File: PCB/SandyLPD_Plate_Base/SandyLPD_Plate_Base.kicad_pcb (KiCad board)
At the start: 2 copper layers, 131 x 83 mm, 78 parts

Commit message: 不要部品削除
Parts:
- removed G***: LOGO, locallib:SandyLP_QR_360dpi
- removed LOGO1: Logo_Base, locallib:SandyLP_logo_LP40_w60
- removed the REF** at (63.8, 81.4)
- removed the REF** at (14.5, 44.3)
- removed the REF** at (107.9, 111.1)
- removed the REF** at (290.6, 44.5)
- removed the REF** at (161.1, 97.0)
- removed the REF** at (209.1, 44.5)
- removed the REF** at (190.1, 14.5)
- removed the REF** at (161.6, 46.6)
- removed the REF** at (269.9, 18.1)
- removed the REF** at (97.4, 22.1)
- removed the REF** at (270.5, 19.6)
- removed the REF** at (97.4, 22.0)
- removed the REF** at (308.0, 47.0)
- removed the REF** at (125.3, 60.8)
- removed the REF** at (308.8, 53.8)
- removed the REF** at (92.0, 130.3)
- removed the REF** at (209.1, 44.6)
- removed the REF** at (110.6, 24.6)
- removed the REF** at (305.1, 37.1)
- removed the REF** at (121.1, 24.6)
- removed the REF** at (159.5, 88.1)
- removed the REF** at (63.3, 81.5)
- removed the REF** at (18.1, 119.3)
- removed the REF** at (121.6, 26.2)
- removed the REF** at (190.6, 16.1)
- removed the REF** at (194.1, 60.8)
- removed the REF** at (4.39, 31.8)
- removed the REF** at (14.0, 51.6)
- removed the REF** at (254.4, 81.5)
- removed the REF** at (158.7, 95.8)
- removed the REF** at (14.6, 44.4)
- removed the REF** at (34.2, 27.6)
- removed the REF** at (305.6, 38.8)
- removed the REF** at (307.8, 111.7)
- removed the REF** at (54.9, 5.36)
- removed the REF** at (54.5, 3.76)
- removed the REF** at (261.0, 37.1)
- removed the REF** at (4.78, 33.4)
- removed the REF** at (159.8, 80.6)
- removed the REF** at (124.6, 59.2)
- removed the REF** at (309.2, 55.6)
- removed the REF** at (111.0, 26.4)
- removed the REF** at (188.2, -4.82)
- removed the REF** at (190.4, 1.58)
- removed the REF** at (209.1, 111.1)
- removed the REF** at (115.1, 26.1)
- removed the REF** at (261.5, 38.8)
- removed the REF** at (193.7, 59.2)
- removed the REF** at (206.2, 132.1)
- removed the REF** at (34.5, 29.9)
- removed the REF** at (14.5, 53.2)
- removed the REF** at (159.4, 78.8)
- removed the REF** at (114.5, 24.6)
- removed the REF** at (16.8, 117.8)
- removed the REF** at (305.6, 114.2)
- removed the REF** at (254.3, 81.4)
- removed the REF** at (159.2, 44.3)
- removed the REF** at (159.7, 87.9)
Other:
- board text removed: "#SandyLP_kbd DN0010, Base by @jpskenn github.com/jpskenn/SandyLP"
- board text removed: "100x100mm"
- board text removed: "Back Side"
- board text removed: "Fairness, Justice, Rightness"
- board text removed: "Screw for SW-plate"
- board text removed: "Screw for Top plate"
- board text removed: "Through-hole tap head diameter"

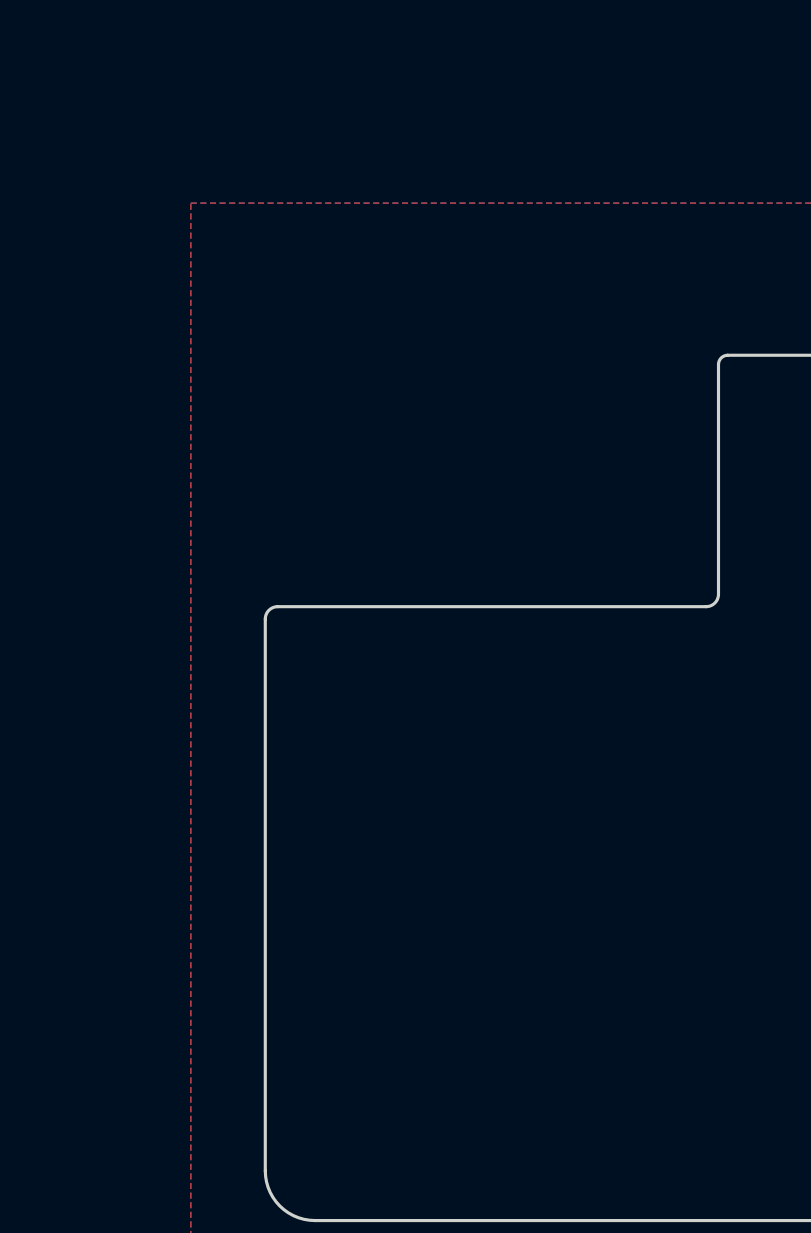
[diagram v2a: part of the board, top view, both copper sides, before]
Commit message: ロータリーエンコーダの穴をちょっと小さく。 #40
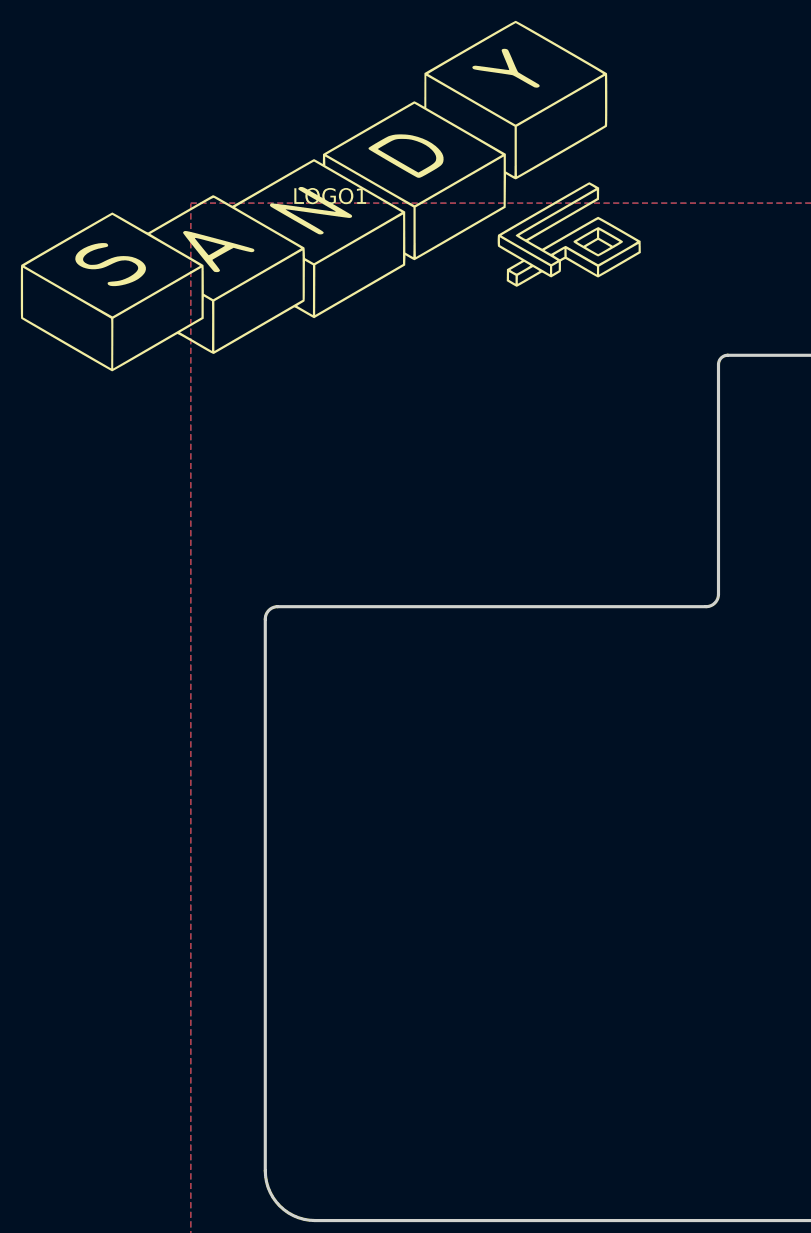
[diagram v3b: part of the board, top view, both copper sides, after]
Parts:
- added LOGO1: Logo_Base, locallib:SandyLP_logo_LP40_w60, F.Cu at (29.7, 16.9)
- SW_13: footprint locallib:MX-Switch-Hole-for-RE(higher hole)-with-narrow-frame -> locallib:MX-Switch-Hole-for-RE(higher hole)-with-narrow-frame-gentle-corner
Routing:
- added copper zone on B.Cu, net (none)
- added copper zone on F.Cu, net (none)
- removed copper zone on B.Cu, net GND
- removed copper zone on F.Cu, net GND

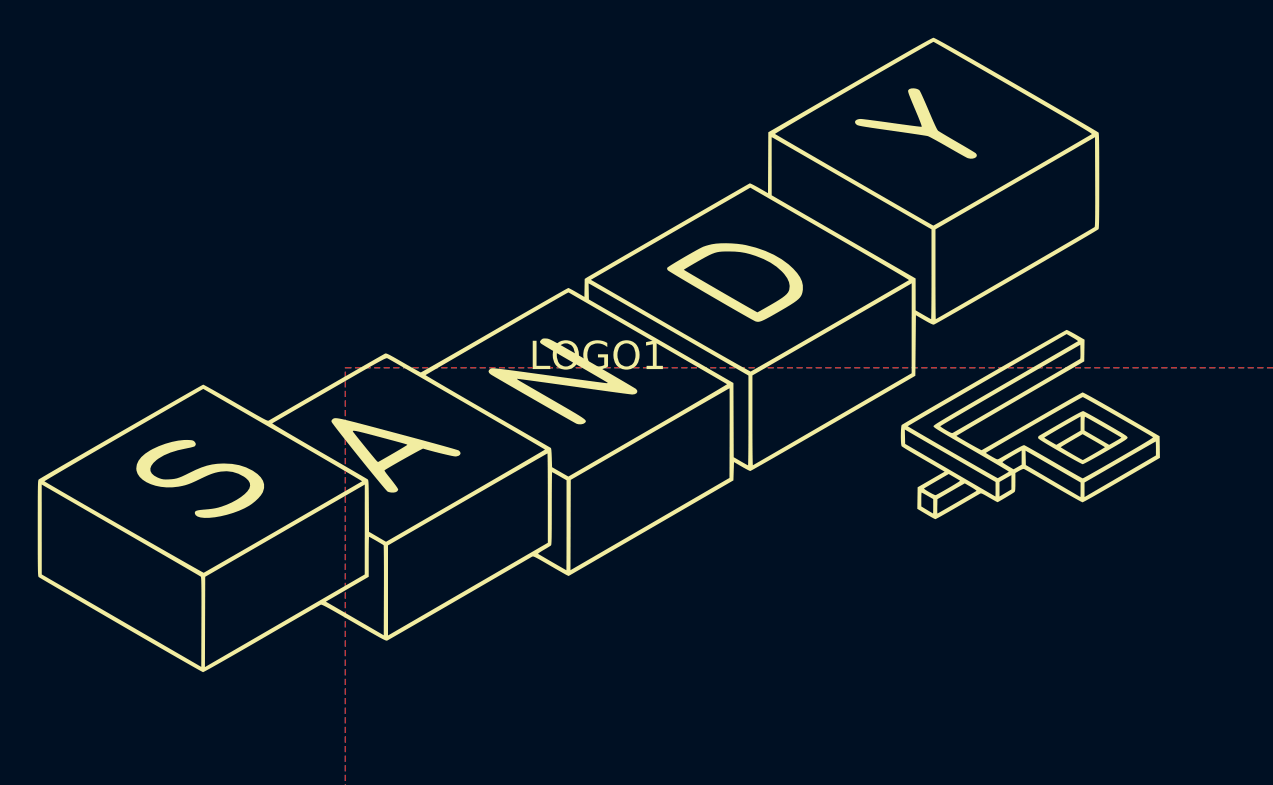
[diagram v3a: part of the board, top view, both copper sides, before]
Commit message: ゴムシート貼り付けめやすを追加
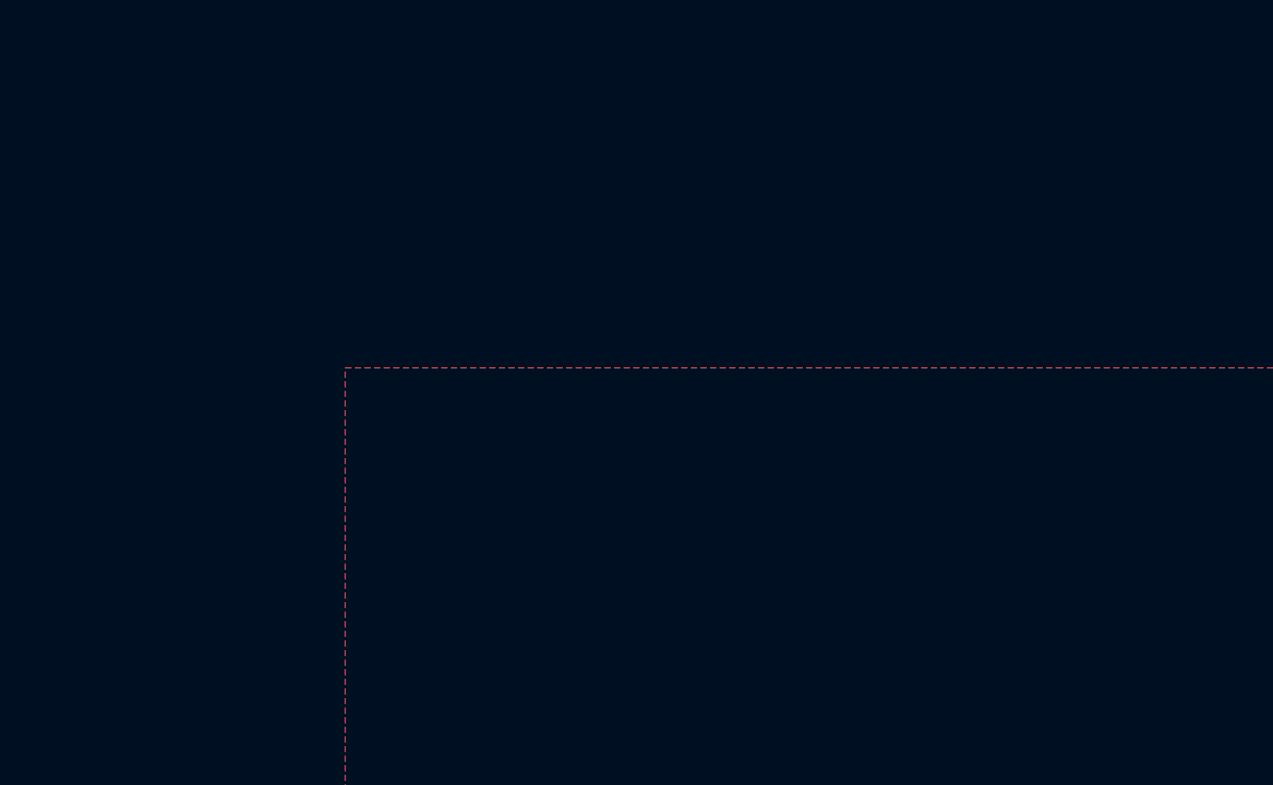
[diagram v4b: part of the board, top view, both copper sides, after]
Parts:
- removed LOGO1: Logo_Base, locallib:SandyLP_logo_LP40_w60
